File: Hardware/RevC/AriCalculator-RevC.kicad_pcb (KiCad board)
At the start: 2 copper layers, 0 parts

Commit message: work in progress
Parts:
- added BAT_?: AAA-Battery, AAA-BATTERY, F.Cu at (106.7, 78.7)
- added BAT_?: AAA-Battery, AAA-BATTERY, F.Cu at (106.7, 200.7)
- added DOGL128-6: VAL**, DOGL128-6, F.Cu at (106.7, 108.0)
- added KEY***: KEY, KEY, F.Cu at (132.1, 195.6)
- added KEY***: KEY, KEY, F.Cu at (132.1, 185.4)
- added KEY***: KEY, KEY, F.Cu at (132.1, 175.3)
- added KEY***: KEY, KEY, F.Cu at (132.1, 165.1)
- added KEY***: KEY, KEY, F.Cu at (132.1, 154.9)
- added KEY***: KEY, KEY, F.Cu at (132.1, 144.8)
- added enclosure: VAL**, enclosure, F.Cu at (68.6, 66.0)
- added switch: SW**, switch, F.Cu at (139.7, 132.1)
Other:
- board outline added: 76.2 x 147.3 mm

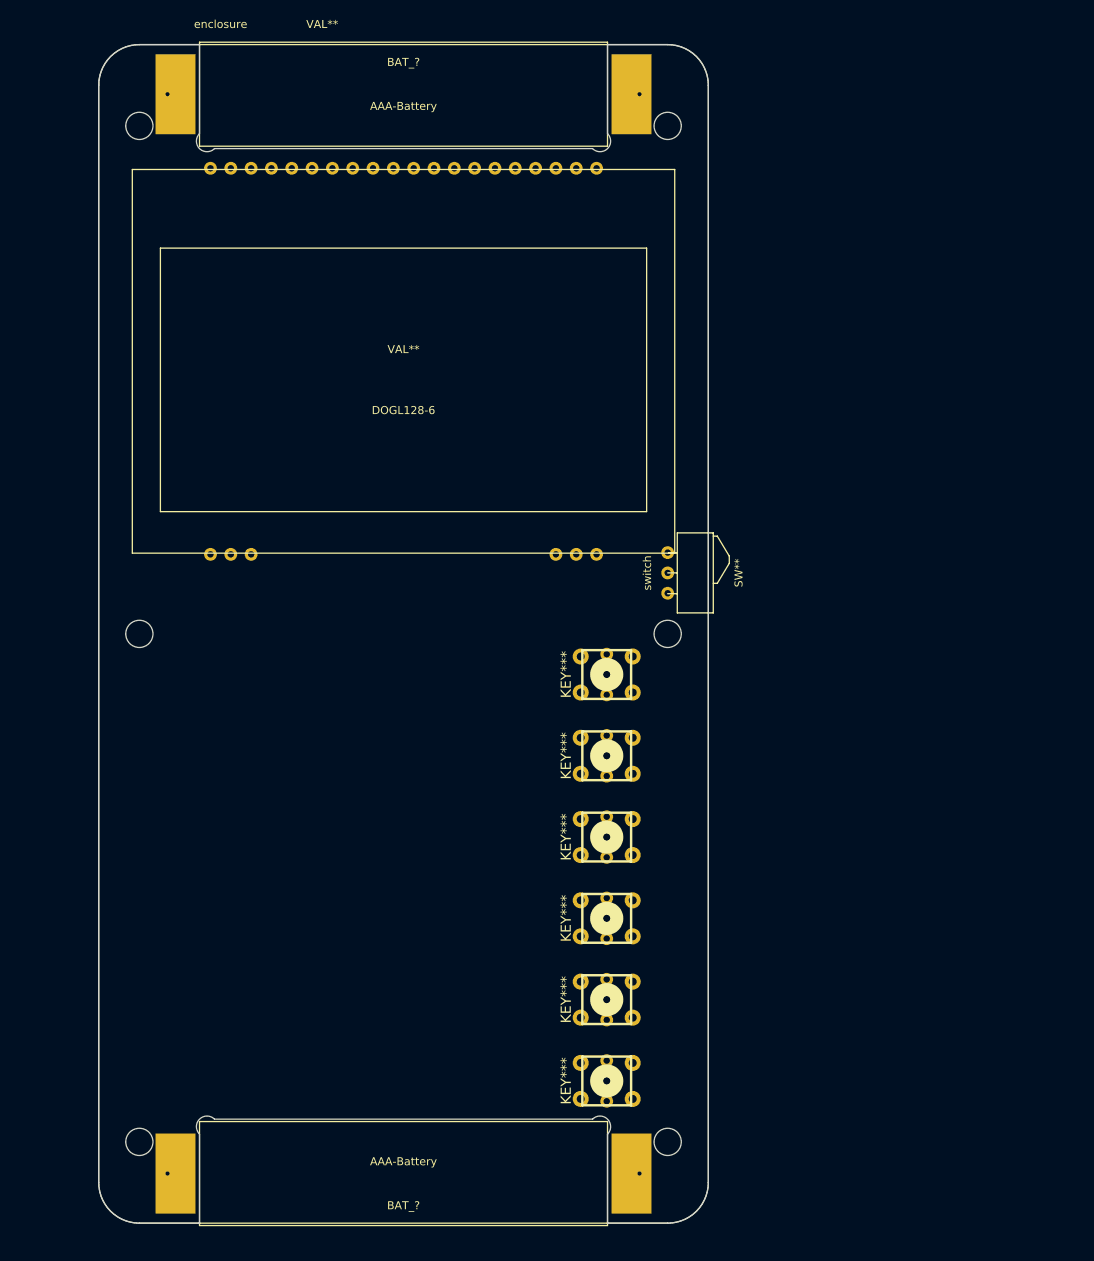
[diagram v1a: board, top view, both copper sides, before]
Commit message: started RevC layout
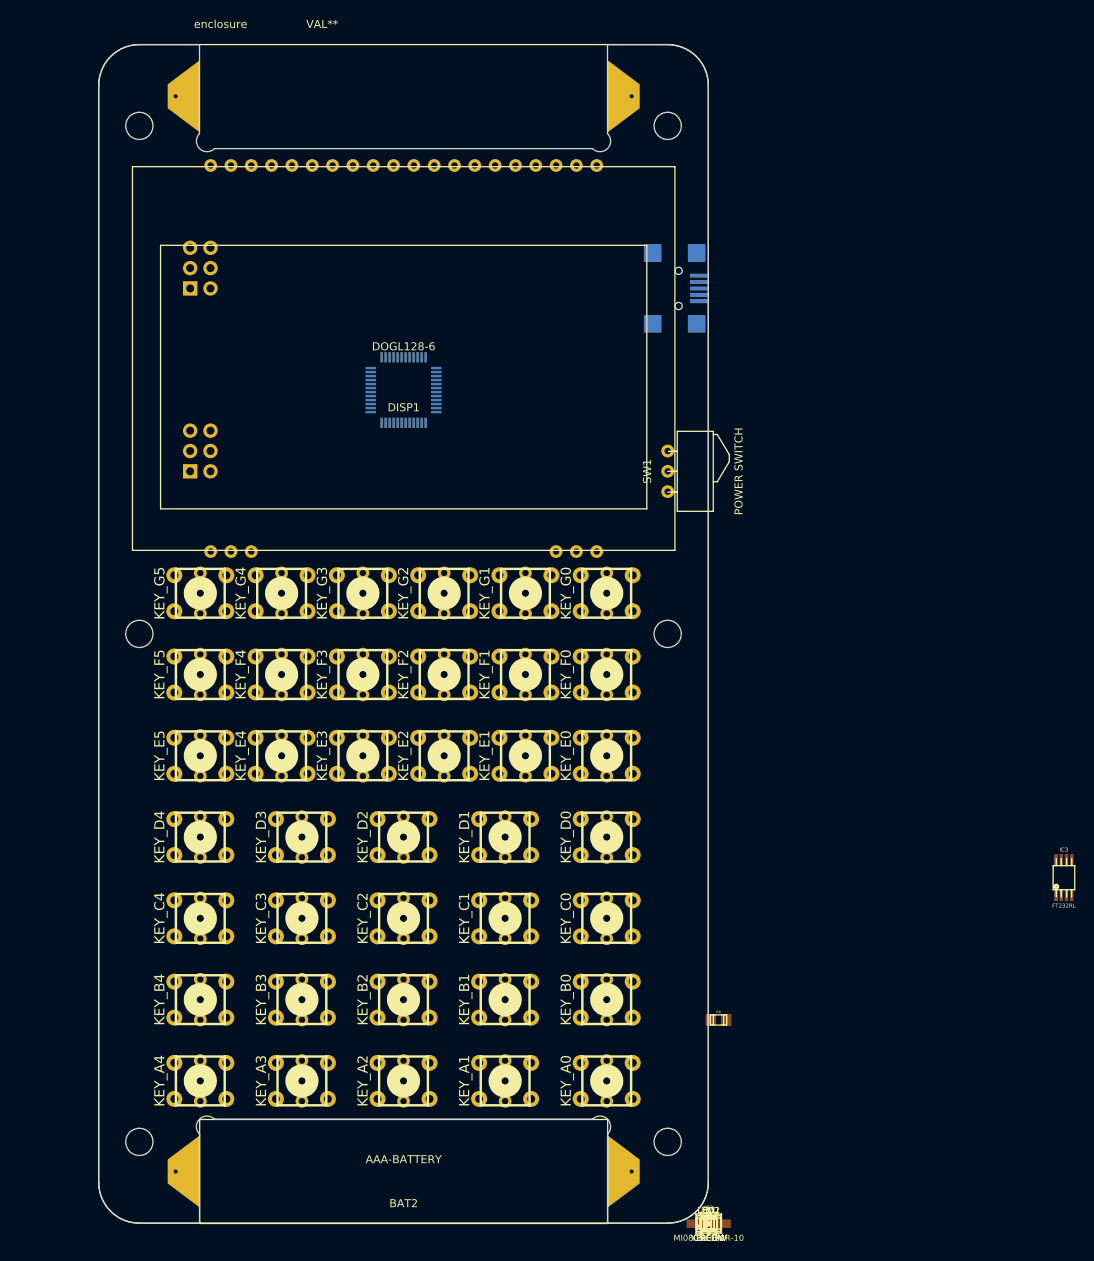
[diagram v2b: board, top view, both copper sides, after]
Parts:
- removed BAT_? (x2): AAA-Battery, AAA-BATTERY
- removed DOGL128-6: VAL**, DOGL128-6
- removed KEY*** (x6): KEY, KEY
- removed switch: SW**, switch
- added BAT1: AAA-BATTERY, AAA-BATTERY, B.Cu at (106.7, 79.0)
- added BAT2: AAA-BATTERY, AAA-BATTERY, F.Cu at (106.7, 200.4)
- added C1: 100nf, c_0805, F.Cu at (144.8, 213.4)
- added C10, C11, C12, C5, C6, C7, C8, C9: 1uF, c_0805, F.Cu at (144.8, 213.4)
- added C13: 1uf, c_0805, F.Cu at (144.8, 213.4)
- added C15: 10nF, c_0805, F.Cu at (144.8, 213.4)
- added C16, C3: 4.7uF, c_0805, F.Cu at (144.8, 213.4)
- added C17, C18, C2: 100nF, c_0805, F.Cu at (144.8, 213.4)
- added C4: 10uF, c_0805, F.Cu at (144.8, 213.4)
- added CON1: BDM, pin_strip_3x2-90, B.Cu at (81.3, 116.8)
- added CON2: SPI, pin_strip_3x2-90, B.Cu at (81.3, 94.0)
- added CON3: USB-MINI-B, conn_usb_B_mini_smd, B.Cu at (139.7, 96.5)
- added D1: YELLOW, Led_0805, F.Cu at (144.8, 213.4)
- added DISP1: DOGL128-6, DOGL128-6, F.Cu at (106.7, 107.6)
- added FB1: MI0805K400R-10, inductor_smd_0805, F.Cu at (144.8, 213.4)
- added IC1: MC9S12G, lqfp48, B.Cu at (106.7, 109.2)
- added IC2: MCP1640, sot23-6, F.Cu at (144.8, 213.4)
- added IC3: FT232RL, msop-8, F.Cu at (189.2, 170.2)
- added KEY_A0: KEY, KEY, F.Cu at (132.1, 195.6)
- added KEY_A1: KEY, KEY, F.Cu at (119.4, 195.6)
- added KEY_A2: KEY, KEY, F.Cu at (106.7, 195.6)
- added KEY_A3: KEY, KEY, F.Cu at (94.0, 195.6)
- added KEY_A4: KEY, KEY, F.Cu at (81.3, 195.6)
- added KEY_B0: KEY, KEY, F.Cu at (132.1, 185.4)
- added KEY_B1: KEY, KEY, F.Cu at (119.4, 185.4)
- added KEY_B2: KEY, KEY, F.Cu at (106.7, 185.4)
- added KEY_B3: KEY, KEY, F.Cu at (94.0, 185.4)
- added KEY_B4: KEY, KEY, F.Cu at (81.3, 185.4)
- added KEY_C0: KEY, KEY, F.Cu at (132.1, 175.3)
- added KEY_C1: KEY, KEY, F.Cu at (119.4, 175.3)
- added KEY_C2: KEY, KEY, F.Cu at (106.7, 175.3)
- added KEY_C3: KEY, KEY, F.Cu at (94.0, 175.3)
- added KEY_C4: KEY, KEY, F.Cu at (81.3, 175.3)
- added KEY_D0: KEY, KEY, F.Cu at (132.1, 165.1)
- added KEY_D1: KEY, KEY, F.Cu at (119.4, 165.1)
- added KEY_D2: KEY, KEY, F.Cu at (106.7, 165.1)
- added KEY_D3: KEY, KEY, F.Cu at (94.0, 165.1)
- added KEY_D4: KEY, KEY, F.Cu at (81.3, 165.1)
- added KEY_E0: KEY, KEY, F.Cu at (132.1, 154.9)
- added KEY_E1: KEY, KEY, F.Cu at (121.9, 154.9)
- added KEY_E2: KEY, KEY, F.Cu at (111.8, 154.9)
- added KEY_E3: KEY, KEY, F.Cu at (101.6, 154.9)
- added KEY_E4: KEY, KEY, F.Cu at (91.4, 154.9)
- added KEY_E5: KEY, KEY, F.Cu at (81.3, 154.9)
- added KEY_F0: KEY, KEY, F.Cu at (132.1, 144.8)
- added KEY_F1: KEY, KEY, F.Cu at (121.9, 144.8)
- added KEY_F2: KEY, KEY, F.Cu at (111.8, 144.8)
- added KEY_F3: KEY, KEY, F.Cu at (101.6, 144.8)
- added KEY_F4: KEY, KEY, F.Cu at (91.4, 144.8)
- added KEY_F5: KEY, KEY, F.Cu at (81.3, 144.8)
- added KEY_G0: KEY, KEY, F.Cu at (132.1, 134.6)
- added KEY_G1: KEY, KEY, F.Cu at (121.9, 134.6)
- added KEY_G2: KEY, KEY, F.Cu at (111.8, 134.6)
- added KEY_G3: KEY, KEY, F.Cu at (101.6, 134.6)
- added KEY_G4: KEY, KEY, F.Cu at (91.4, 134.6)
- added KEY_G5: KEY, KEY, F.Cu at (81.3, 134.6)
- added L1: 4.7uH, lqh3c, F.Cu at (144.8, 213.4)
- added LED1: GREEN, Led_0805, F.Cu at (144.8, 213.4)
- added LED2: RED, Led_0805, F.Cu at (144.8, 213.4)
- added R1, R13, R2: 120, r_0805, F.Cu at (144.8, 213.4)
- added R10: 470K, r_0805, F.Cu at (144.8, 213.4)
- added R11: 4K7, r_0805, F.Cu at (144.8, 213.4)
- added R12: 10K, r_0805, F.Cu at (144.8, 213.4)
- added R3, R4, R5, R6, R7: 100, r_0805, F.Cu at (144.8, 213.4)
- added R8: 100, r_0805, F.Cu at (146.1, 188.0)
- added R9: 820K, r_0805, F.Cu at (144.8, 213.4)
- added SW1: POWER SWITCH, switch, F.Cu at (139.7, 119.4)

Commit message: work in progress
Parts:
- C1, C10, C11, C12, C13, C15, C16, C17, C2, C5, C6, C7, C8, C9, FB1, IC2, R11, R12, R13: moved to B.Cu
- IC3: footprint msop-8 -> ssop-28; moved to B.Cu
- moved L1 140.0 mm to (153.7, 73.7)
- moved C8 136.5 mm to (101.5, 84.0)
- moved C7 135.1 mm to (106.0, 84.0), turned to 180 degrees
- moved C6 133.9 mm to (110.5, 84.0)
- moved C5 132.8 mm to (115.0, 84.0)
- moved C9 130.7 mm to (120.5, 85.0), turned to 270 degrees
- moved C10 130.3 mm to (123.0, 85.0), turned to 270 degrees
- moved C11 129.9 mm to (125.5, 85.0), turned to 270 degrees
- moved C12 129.5 mm to (128.0, 85.0), turned to 270 degrees
- moved C13 129.2 mm to (130.5, 85.0), turned to 270 degrees
- moved C3 123.9 mm to (166.4, 91.4)
- moved R3 123.3 mm to (175.3, 94.0)
- moved D1 121.3 mm to (70.5, 117.5), turned to 270 degrees
- moved R9 121.2 mm to (156.2, 92.7)
- moved R12 120.0 mm to (85.2, 109.2), turned to 180 degrees
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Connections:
- BAT1 pad 1: N-0000096 (its old number) -> N-0000095
- CON1 pad 2: (no net) -> GND
- KEY_A3 pad 2: N-0000093 (its old number) -> /Keypad/KEYPAD_COL_3
- KEY_B3 pad 2: N-0000093 (its old number) -> /Keypad/KEYPAD_COL_3
- KEY_B3 pad 4: N-0000093 (its old number) -> /Keypad/KEYPAD_COL_3
- KEY_B3 pad 6: N-0000093 (its old number) -> /Keypad/KEYPAD_COL_3
- KEY_C3 pad 2: N-0000093 (its old number) -> /Keypad/KEYPAD_COL_3
- KEY_C3 pad 4: N-0000093 (its old number) -> /Keypad/KEYPAD_COL_3
- KEY_C3 pad 6: N-0000093 (its old number) -> /Keypad/KEYPAD_COL_3
- KEY_D3 pad 2: N-0000093 (its old number) -> /Keypad/KEYPAD_COL_3
- KEY_D3 pad 4: N-0000093 (its old number) -> /Keypad/KEYPAD_COL_3
- KEY_D3 pad 6: N-0000093 (its old number) -> /Keypad/KEYPAD_COL_3
- KEY_E3 pad 2: N-0000093 (its old number) -> /Keypad/KEYPAD_COL_3
- KEY_E3 pad 4: N-0000093 (its old number) -> /Keypad/KEYPAD_COL_3
- KEY_E3 pad 6: N-0000093 (its old number) -> /Keypad/KEYPAD_COL_3
- KEY_F3 pad 2: N-0000093 (its old number) -> /Keypad/KEYPAD_COL_3
- KEY_F3 pad 4: N-0000093 (its old number) -> /Keypad/KEYPAD_COL_3
- KEY_F3 pad 6: N-0000093 (its old number) -> /Keypad/KEYPAD_COL_3
- KEY_G3 pad 2: N-0000093 (its old number) -> /Keypad/KEYPAD_COL_3
- KEY_G3 pad 4: N-0000093 (its old number) -> /Keypad/KEYPAD_COL_3
- KEY_G3 pad 6: N-0000093 (its old number) -> /Keypad/KEYPAD_COL_3
- SW1 pad 1: GND -> N-0000095
- SW1 pad 3: N-0000096 (its old number) -> GND
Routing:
- net /Keypad/KEYPAD_ROW_A: track 0.00 -> 158.9 mm
- net /Keypad/KEYPAD_COL_0: track 0.00 -> 150.3 mm
- net /Keypad/KEYPAD_COL_4: track 0.00 -> 149.2 mm, vias 0 -> 1
- net /Keypad/KEYPAD_ROW_B: track 0.00 -> 144.6 mm
- net /Keypad/KEYPAD_COL_1: track 0.00 -> 141.9 mm
- net /Keypad/KEYPAD_COL_3: track 0.00 -> 137.6 mm, vias 0 -> 1
- net /Keypad/KEYPAD_COL_2: track 0.00 -> 131.9 mm, vias 0 -> 1
- net /Keypad/KEYPAD_ROW_F: track 0.00 -> 105.0 mm
- net /Keypad/KEYPAD_ROW_G: track 0.00 -> 97.7 mm
- net /Keypad/KEYPAD_COL_5: track 0.00 -> 90.4 mm, vias 0 -> 1
- net /Keypad/KEYPAD_ROW_C: track 0.00 -> 87.4 mm
- net /Keypad/KEYPAD_ROW_E: track 0.00 -> 84.0 mm
- net /Keypad/KEYPAD_ROW_D: track 0.00 -> 68.7 mm
- net N-0000092: track 0.00 -> 16.8 mm, vias 0 -> 1
- net VUSB: track 0.00 -> 16.2 mm
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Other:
- outline, holes or cut-outs redrawn
- net class Analog added: clearance 0.2, trace_width 0.4, via_dia 0.5, via_drill 0.3
- net class Default: clearance 0.254 -> 0.2; trace_width 0.254 -> 0.2; via_dia 0.889 -> 0.5; via_drill 0.635 -> 0.3
- rule trace_clearance: 0.254 -> 0.2
- rule trace_min: 0.254 -> 0.1524
- rule via_min_drill: 0.508 -> 0.3
- rule via_min_size: 0.889 -> 0.5

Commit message: work in progress
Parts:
- added C19: 10uF, c_0805, F.Cu at (177.8, 102.9)
- added C20: 20uF, c_0805, F.Cu at (163.8, 100.3)
- added IC4: MCP1643, msop-8, F.Cu at (154.9, 88.9)
- added L2: 4.7uH, lqh3c, F.Cu at (162.6, 87.6)
- added LED10: BACKLIGHT, Led_1206, F.Cu at (161.3, 128.3)
- added LED11: BACKLIGHT, Led_1206, F.Cu at (160.0, 116.8)
- added LED12: BACKLIGHT, Led_1206, F.Cu at (170.2, 111.8)
- added LED13: BACKLIGHT, Led_1206, F.Cu at (160.0, 110.5)
- added LED14: BACKLIGHT, Led_1206, F.Cu at (170.2, 106.7)
- added LED15: BACKLIGHT, Led_1206, F.Cu at (160.0, 105.4)
- added LED16: BACKLIGHT, Led_1206, F.Cu at (171.4, 134.6)
- added LED17: BACKLIGHT, Led_1206, F.Cu at (171.4, 128.3)
- added LED18: BACKLIGHT, Led_1206, F.Cu at (171.4, 123.2)
- added LED19: BACKLIGHT, Led_1206, F.Cu at (170.2, 118.1)
- added LED20: IR, led_5mm_bend, B.Cu at (78.7, 88.9)
- added LED21: IR, led_5mm_bend, B.Cu at (134.6, 88.9)
- added LED3: YELLOW, Led_0805, F.Cu at (61.0, 118.1)
- added LED4: BACKLIGHT, Led_1206, F.Cu at (166.4, 141.0)
- added LED5: BACKLIGHT, Led_1206, F.Cu at (180.3, 120.7)
- added LED6: BACKLIGHT, Led_1206, F.Cu at (179.1, 125.7)
- added LED7: BACKLIGHT, Led_1206, F.Cu at (179.1, 130.8)
- added LED8: BACKLIGHT, Led_1206, F.Cu at (179.1, 135.9)
- added LED9: BACKLIGHT, Led_1206, F.Cu at (161.3, 134.6)
- added spark_gap_pad_0.8: SG, spark_gap_pad_0.8, B.Cu at (73.6, 113.0)
- added spark_gap_pad_0.8: SG, spark_gap_pad_0.8, B.Cu at (79.4, 120.7)
- added spark_gap_pad_0.8: SG, spark_gap_pad_0.8, B.Cu at (73.6, 122.0)
- added spark_gap_pad_0.8: SG, spark_gap_pad_0.8, B.Cu at (72.8, 113.0)
- added spark_gap_pad_0.8: SG, spark_gap_pad_0.8, B.Cu at (72.8, 122.0)
- added spark_gap_pad_0.8: SG, spark_gap_pad_0.8, B.Cu at (79.4, 117.5)
- added spark_gap_pad_0.8: SG, spark_gap_pad_0.8, B.Cu at (79.4, 118.3)
- added spark_gap_pad_0.8: SG, spark_gap_pad_0.8, B.Cu at (79.4, 116.7)
- added spark_gap_pad_0.8: SG, spark_gap_pad_0.8, B.Cu at (79.4, 119.1)
- added spark_gap_pad_0.8: SG, spark_gap_pad_0.8, B.Cu at (79.4, 119.9)
- BAT2, C18, C3, C4, L1, R10, R3, R4, R5, R6, R7, R8, R9: moved to B.Cu
- moved R3 93.7 mm to (86.8, 124.8), turned to 270 degrees
- moved R7 84.9 mm to (88.9, 124.8), turned to 90 degrees
- moved R6 73.1 mm to (93.0, 124.8), turned to 270 degrees
- moved R5 66.8 mm to (91.0, 124.8), turned to 270 degrees
- moved C18 65.7 mm to (84.2, 110.1), turned to 270 degrees
- moved R4 59.0 mm to (95.1, 124.8), turned to 270 degrees
- moved L1 50.1 mm to (124.0, 114.0)
- moved C3 49.0 mm to (125.5, 118.5)
- moved R10 48.5 mm to (129.5, 111.8)
- moved R1 45.1 mm to (117.4, 125.2)
- moved R2 44.0 mm to (116.8, 122.3)
- moved LED2 37.2 mm to (142.7, 131.7), turned to 270 degrees
- moved R8 36.8 mm to (84.7, 124.9), turned to 90 degrees
- moved LED1 32.9 mm to (140.0, 131.7), turned to 90 degrees
- moved R9 32.7 mm to (127.0, 107.5)
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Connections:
- CON3 pad 2: N-0000083 (its old number) -> /UART/USBD-
- CON3 pad 3: N-0000091 (its old number) -> /UART/USBD+
- D1 pad 2: N-0000092 (its old number) -> N-0000090
- DISP1 pad 1: (no net) -> N-0000068
- DISP1 pad 18: (no net) -> N-0000067
- DISP1 pad 19: (no net) -> N-0000067
- DISP1 pad 2: (no net) -> N-0000068
- DISP1 pad 20: (no net) -> N-0000067
- DISP1 pad 3: (no net) -> N-0000068
- IC1 pad 19: (no net) -> /Display/DISPLAY_BACKLIGHT
- IC3 pad 13: N-0000092 (its old number) -> N-0000088
- IC3 pad 15: N-0000091 (its old number) -> /UART/USBD+
- IC3 pad 16: N-0000083 (its old number) -> /UART/USBD-
- R13 pad 1: N-0000082 -> N-0000085
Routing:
- net /Keypad/KEYPAD_ROW_D: track 68.7 -> 107.3 mm
- net /Keypad/KEYPAD_COL_5: track 90.4 -> 124.0 mm
- net /Keypad/KEYPAD_COL_4: track 149.2 -> 181.1 mm
- net /Keypad/KEYPAD_ROW_A: track 158.9 -> 130.3 mm
- net /Keypad/KEYPAD_ROW_C: track 87.4 -> 112.0 mm
- net /Keypad/KEYPAD_ROW_B: track 144.6 -> 120.7 mm
- net /Keypad/KEYPAD_COL_1: track 141.9 -> 123.5 mm
- net /Keypad/KEYPAD_COL_3: track 137.6 -> 155.4 mm
- net N-0000092 (its old number): track 16.8 -> 0.00 mm, vias 1 -> 0
- net /Keypad/KEYPAD_ROW_G: track 97.7 -> 81.2 mm
- net /Keypad/KEYPAD_ROW_E: track 84.0 -> 99.7 mm
- net /Keypad/KEYPAD_ROW_F: track 105.0 -> 91.1 mm
- net N-0000082: track 12.2 -> 0.00 mm, vias 1 -> 0
- net N-0000083 (its old number): track 10.6 -> 0.00 mm
- net /UART/USBD-: track 0.00 -> 10.6 mm
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- added copper zone on B.Cu, net GND
- added copper zone on F.Cu, net GND
- added copper zone on F.Cu, net N-0000093
- added copper zone on F.Cu, net N-0000094
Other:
- outline, holes or cut-outs redrawn
- net class Analog removed
- net class Default: clearance 0.2 -> 0.16; via_dia 0.5 -> 0.62
- rule trace_clearance: 0.2 -> 0.16
- rule trace_min: 0.1524 -> 0.1523
- rule via_min_size: 0.5 -> 0.62

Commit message: work in progress
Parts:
- removed D1: YELLOW, Led_0805
- added ?: , VIA, F.Cu at (80.4, 119.1)
- added R14: 0.66, r_1206, F.Cu at (157.2, 97.4)
- added spark_gap_pad_0.8: SG, spark_gap_pad_0.8, F.Cu at (71.8, 199.4)
- added spark_gap_pad_0.8: SG, spark_gap_pad_0.8, F.Cu at (141.7, 80.0)
- added spark_gap_pad_0.8: SG, spark_gap_pad_0.8, F.Cu at (142.4, 80.0)
- added spark_gap_pad_0.8: SG, spark_gap_pad_0.8, F.Cu at (71.0, 199.4)
- added spark_gap_pad_0.8: SG, spark_gap_pad_0.8, B.Cu at (141.1, 111.3)
- added spark_gap_pad_0.8: SG, spark_gap_pad_0.8, B.Cu at (141.2, 110.3)
- added spark_gap_pad_0.8: SG, spark_gap_pad_0.8, F.Cu at (71.0, 80.0)
- added spark_gap_pad_0.8: SG, spark_gap_pad_0.8, F.Cu at (71.8, 80.0)
- moved L1 13.6 mm to (136.4, 119.7), turned to 270 degrees
- moved LED3 11.1 mm to (72.0, 117.5), turned to 270 degrees
- moved R10 10.5 mm to (130.4, 122.2)
- moved IC2 3.85 mm to (133.2, 118.4), turned to 180 degrees
- moved L2 1.54 mm to (162.7, 86.1)
- moved C4 1.53 mm to (134.7, 111.5)
- moved spark_gap_pad_0.8 0.58 mm to (73.9, 112.5)
- moved spark_gap_pad_0.8 0.58 mm to (73.9, 122.5)
- moved spark_gap_pad_0.8 0.58 mm to (73.1, 122.5)
- moved spark_gap_pad_0.8 0.58 mm to (73.1, 112.5)
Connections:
- CON3 pad 6: (no net) -> N-0000073
- CON3 pad 7: (no net) -> N-0000074
- CON3 pad 8: (no net) -> N-0000075
- CON3 pad 9: (no net) -> N-0000071
- spark_gap_pad_0.8 pad : (no net) -> N-0000075
- spark_gap_pad_0.8 pad : (no net) -> N-0000074
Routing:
- net N-0000075: track 0.00 -> 1.72 mm
- net N-0000074: track 0.00 -> 1.72 mm
